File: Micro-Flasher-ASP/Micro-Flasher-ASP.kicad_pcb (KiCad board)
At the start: 2 copper layers, 56.4 x 23 mm, 2 parts, among them J1 Conn_02x03_Odd_Even, U1 ProMicro

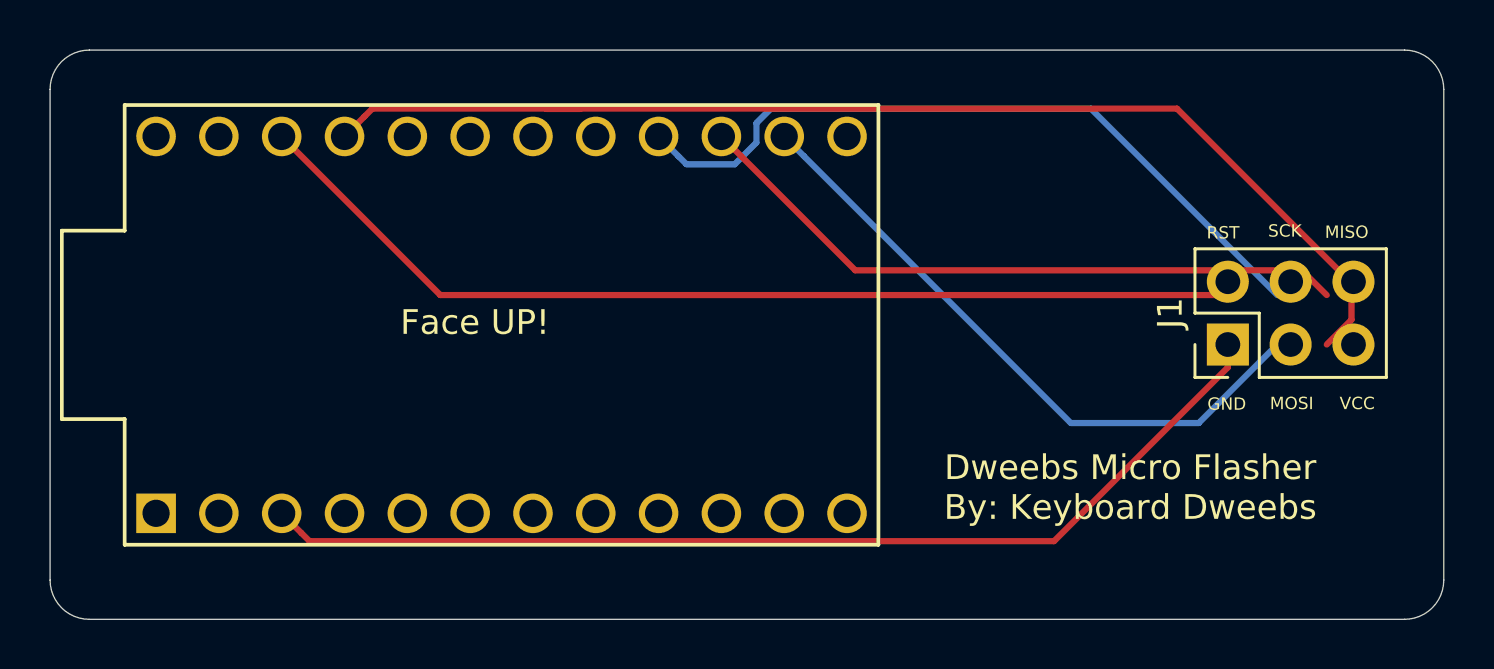
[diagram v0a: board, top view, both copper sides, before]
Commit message: fixed unconnected routes
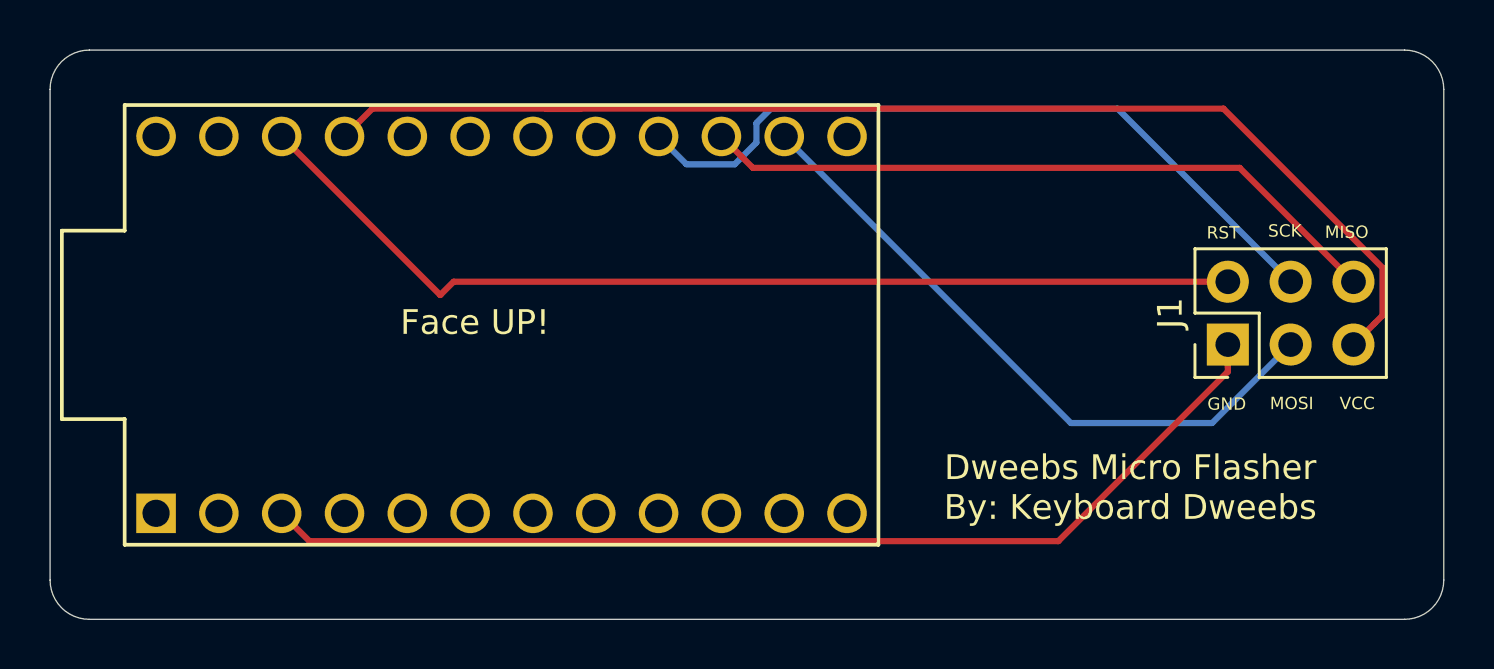
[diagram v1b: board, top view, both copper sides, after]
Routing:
- net Net-(J1-Pad5): track 47.0 -> 48.7 mm
- net Net-(J1-Pad1): track 42.6 -> 43.6 mm
- net Net-(J1-Pad6): track 27.1 -> 28.0 mm
- net Net-(J1-Pad3): track 26.1 -> 26.6 mm
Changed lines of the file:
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@@
     (thickness 1.6)
     (drawings 16)
-    (tracks 33)
+    (tracks 32)
     (zones 0)
     (modules 2)
@@
   )
   (segment (start 123.989999 56.679999) (end 123.19 55.88) (width 0.25) (layer F.Cu) (net 1))
-  (segment (start 128.603749 61.293749) (end 123.989999 56.679999) (width 0.25) (layer F.Cu) (net 1))
-  (segment (start 146.668749 61.293749) (end 128.603749 61.293749) (width 0.25) (layer F.Cu) (net 1))
-  (segment (start 147.66875 62.29375) (end 146.668749 61.293749) (width 0.25) (layer F.Cu) (net 1))
-  (segment (start 108.749999 55.080001) (end 107.95 55.88) (width 0.25) (layer F.Cu) (net 2))
-  (segment (start 109.075001 54.754999) (end 108.749999 55.080001) (width 0.25) (layer F.Cu) (net 2))
-  (segment (start 116.110001 54.754999) (end 109.075001 54.754999) (width 0.25) (layer F.Cu) (net 2))
-  (segment (start 116.123752 54.76875) (end 116.110001 54.754999) (width 0.25) (layer F.Cu) (net 2))
-  (segment (start 117.475 54.76875) (end 116.123752 54.76875) (width 0.25) (layer F.Cu) (net 2))
-  (segment (start 117.488751 54.754999) (end 117.475 54.76875) (width 0.25) (layer F.Cu) (net 2))
-  (segment (start 148.668751 61.813749) (end 141.610001 54.754999) (width 0.25) (layer F.Cu) (net 2))
-  (segment (start 148.668751 63.293749) (end 148.668751 61.813749) (width 0.25) (layer F.Cu) (net 2))
-  (segment (start 141.610001 54.754999) (end 117.488751 54.754999) (width 0.25) (layer F.Cu) (net 2))
-  (segment (start 147.66875 64.29375) (end 148.668751 63.293749) (width 0.25) (layer F.Cu) (net 2))
-  (segment (start 121.775001 57.005001) (end 121.449999 56.679999) (width 0.25) (layer B.Cu) (net 3))
-  (segment (start 123.730001 57.005001) (end 121.775001 57.005001) (width 0.25) (layer B.Cu) (net 3))
-  (segment (start 124.604999 56.130003) (end 123.730001 57.005001) (width 0.25) (layer B.Cu) (net 3))
-  (segment (start 121.449999 56.679999) (end 120.65 55.88) (width 0.25) (layer B.Cu) (net 3))
-  (segment (start 124.604999 55.339999) (end 124.604999 56.130003) (width 0.25) (layer B.Cu) (net 3))
-  (segment (start 125.189999 54.754999) (end 124.604999 55.339999) (width 0.25) (layer B.Cu) (net 3))
-  (segment (start 138.129999 54.754999) (end 125.189999 54.754999) (width 0.25) (layer B.Cu) (net 3))
-  (segment (start 145.66875 62.29375) (end 138.129999 54.754999) (width 0.25) (layer B.Cu) (net 3))
-  (segment (start 126.529999 56.679999) (end 125.73 55.88) (width 0.25) (layer B.Cu) (net 4))
-  (segment (start 137.31875 67.46875) (end 126.529999 56.679999) (width 0.25) (layer B.Cu) (net 4))
-  (segment (start 142.49375 67.46875) (end 137.31875 67.46875) (width 0.25) (layer B.Cu) (net 4))
-  (segment (start 145.66875 64.29375) (end 142.49375 67.46875) (width 0.25) (layer B.Cu) (net 4))
+  (segment (start 124.46 57.15) (end 123.989999 56.679999) (width 0.25) (layer F.Cu) (net 1))
+  (segment (start 144.145 57.15) (end 124.46 57.15) (width 0.25) (layer F.Cu) (net 1))
+  (segment (start 148.74875 61.75375) (end 144.145 57.15) (width 0.25) (layer F.Cu) (net 1))
+  (segment (start 149.923751 63.118749) (end 149.598749 63.443751) (width 0.25) (layer F.Cu) (net 2))
+  (segment (start 149.923751 61.189749) (end 149.923751 63.118749) (width 0.25) (layer F.Cu) (net 2))
+  (segment (start 143.489001 54.754999) (end 149.923751 61.189749) (width 0.25) (layer F.Cu) (net 2))
+  (segment (start 107.95 55.88) (end 109.075001 54.754999) (width 0.25) (layer F.Cu) (net 2))
+  (segment (start 109.075001 54.754999) (end 116.110001 54.754999) (width 0.25) (layer F.Cu) (net 2))
+  (segment (start 149.598749 63.443751) (end 148.74875 64.29375) (width 0.25) (layer F.Cu) (net 2))
+  (segment (start 116.110001 54.754999) (end 116.123752 54.76875) (width 0.25) (layer F.Cu) (net 2))
+  (segment (start 116.123752 54.76875) (end 117.475 54.76875) (width 0.25) (layer F.Cu) (net 2))
+  (segment (start 117.475 54.76875) (end 117.488751 54.754999) (width 0.25) (layer F.Cu) (net 2))
+  (segment (start 117.488751 54.754999) (end 143.489001 54.754999) (width 0.25) (layer F.Cu) (net 2))
+  (segment (start 139.209999 54.754999) (end 146.20875 61.75375) (width 0.25) (layer B.Cu) (net 3))
+  (segment (start 121.775001 57.005001) (end 123.730001 57.005001) (width 0.25) (layer B.Cu) (net 3))
+  (segment (start 120.65 55.88) (end 121.775001 57.005001) (width 0.25) (layer B.Cu) (net 3))
+  (segment (start 124.604999 56.130003) (end 124.604999 55.339999) (width 0.25) (layer B.Cu) (net 3))
+  (segment (start 124.604999 55.339999) (end 125.189999 54.754999) (width 0.25) (layer B.Cu) (net 3))
+  (segment (start 123.730001 57.005001) (end 124.604999 56.130003) (width 0.25) (layer B.Cu) (net 3))
+  (segment (start 125.189999 54.754999) (end 139.209999 54.754999) (width 0.25) (layer B.Cu) (net 3))
+  (segment (start 143.03375 67.46875) (end 146.20875 64.29375) (width 0.25) (layer B.Cu) (net 4))
+  (segment (start 125.73 55.88) (end 137.31875 67.46875) (width 0.25) (layer B.Cu) (net 4))
+  (segment (start 137.31875 67.46875) (end 143.03375 67.46875) (width 0.25) (layer B.Cu) (net 4))
   (segment (start 111.82375 62.29375) (end 105.41 55.88) (width 0.25) (layer F.Cu) (net 5))
-  (segment (start 143.66875 62.29375) (end 111.82375 62.29375) (width 0.25) (layer F.Cu) (net 5))
-  (segment (start 106.209999 71.919999) (end 105.41 71.12) (width 0.25) (layer F.Cu) (net 6))
-  (segment (start 106.535001 72.245001) (end 106.209999 71.919999) (width 0.25) (layer F.Cu) (net 6))
-  (segment (start 136.642499 72.245001) (end 106.535001 72.245001) (width 0.25) (layer F.Cu) (net 6))
-  (segment (start 143.66875 65.21875) (end 136.642499 72.245001) (width 0.25) (layer F.Cu) (net 6))
+  (segment (start 112.36375 61.75375) (end 143.66875 61.75375) (width 0.25) (layer F.Cu) (net 5))
+  (segment (start 111.82375 62.29375) (end 112.36375 61.75375) (width 0.25) (layer F.Cu) (net 5))
   (segment (start 143.66875 64.29375) (end 143.66875 65.21875) (width 0.25) (layer F.Cu) (net 6))
+  (segment (start 143.66875 65.39375) (end 143.66875 64.29375) (width 0.25) (layer F.Cu) (net 6))
+  (segment (start 136.817499 72.245001) (end 143.66875 65.39375) (width 0.25) (layer F.Cu) (net 6))
+  (segment (start 106.535001 72.245001) (end 136.817499 72.245001) (width 0.25) (layer F.Cu) (net 6))
+  (segment (start 105.41 71.12) (end 106.535001 72.245001) (width 0.25) (layer F.Cu) (net 6))
 )
